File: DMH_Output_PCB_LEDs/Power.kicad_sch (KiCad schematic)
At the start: 79 parts, among them J0 Conn_01x01, J10 Conn_01x06, J100 IDC_02x05, J23 Conn_01x06, J29 Conn_01x01, U1 TL072, U10 NE5532, U11 TL074, U12 NE5532, U13 NE5532, U14 NE5532, U15 NE5532, U16 NE5532, U17 NE5532, U18 NE5532, U19 NE5532, U2 LM339, U20 TL072, U21 LM4040LP-10, U24 LM339, U25 LM339, U3 LM339, U4 LM339, U5 LM339, U6 LM339, U7 TL072, U8 TL074, U9 NE5532

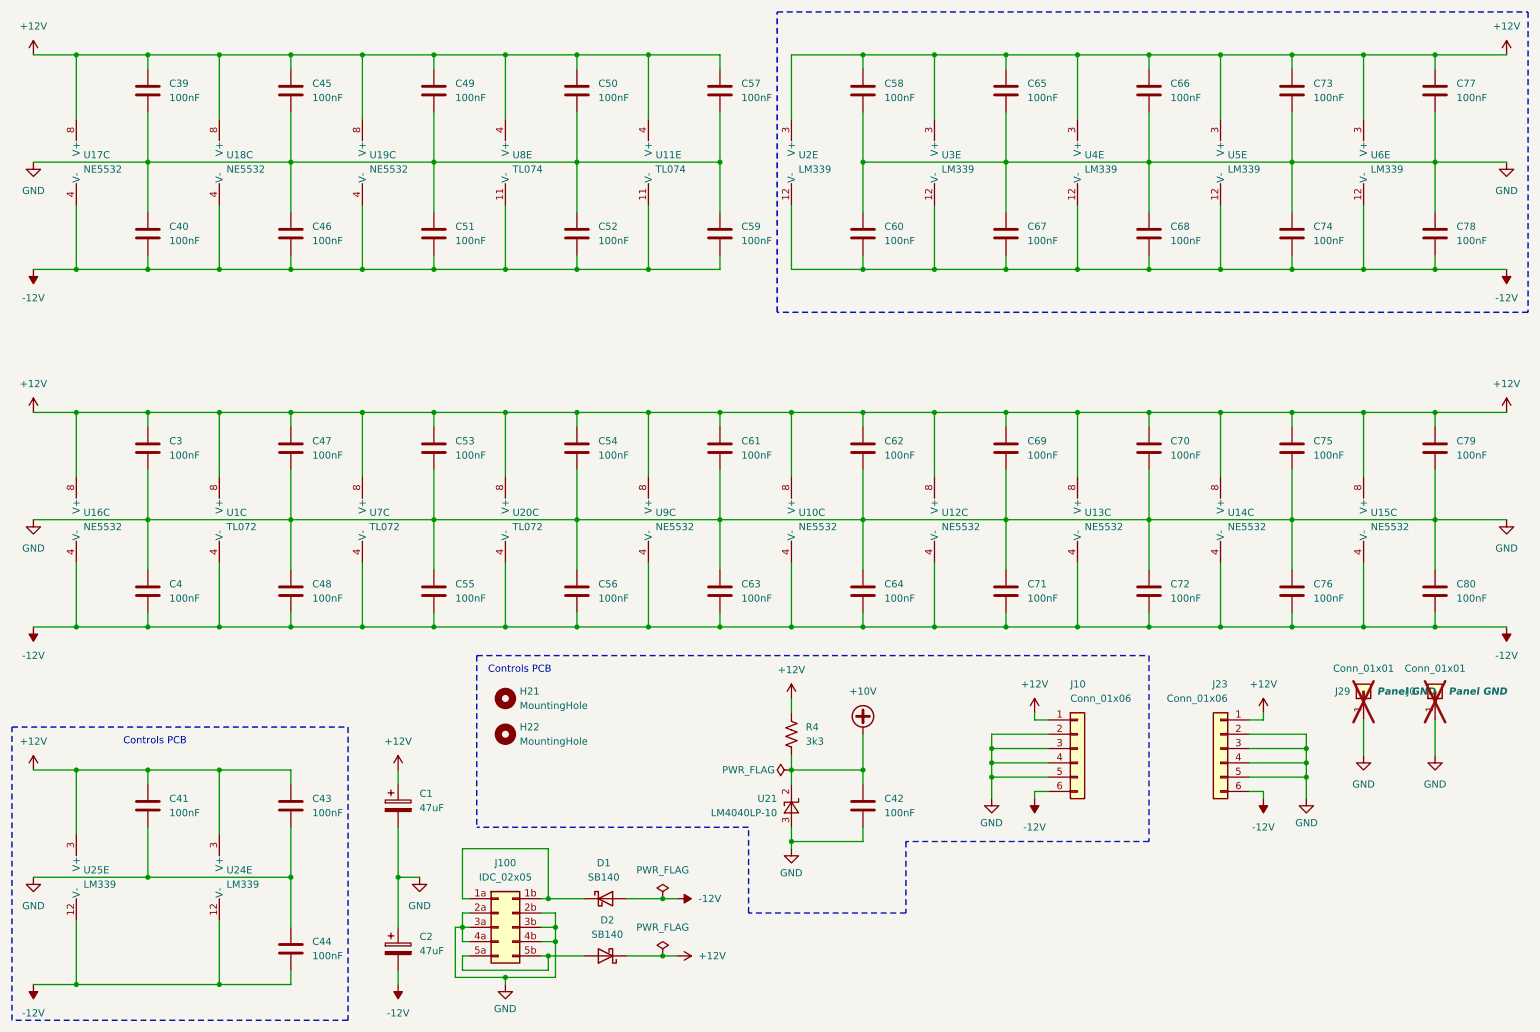
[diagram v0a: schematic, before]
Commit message: Adjusted output meter resistors
... and deleted unnecessary notes
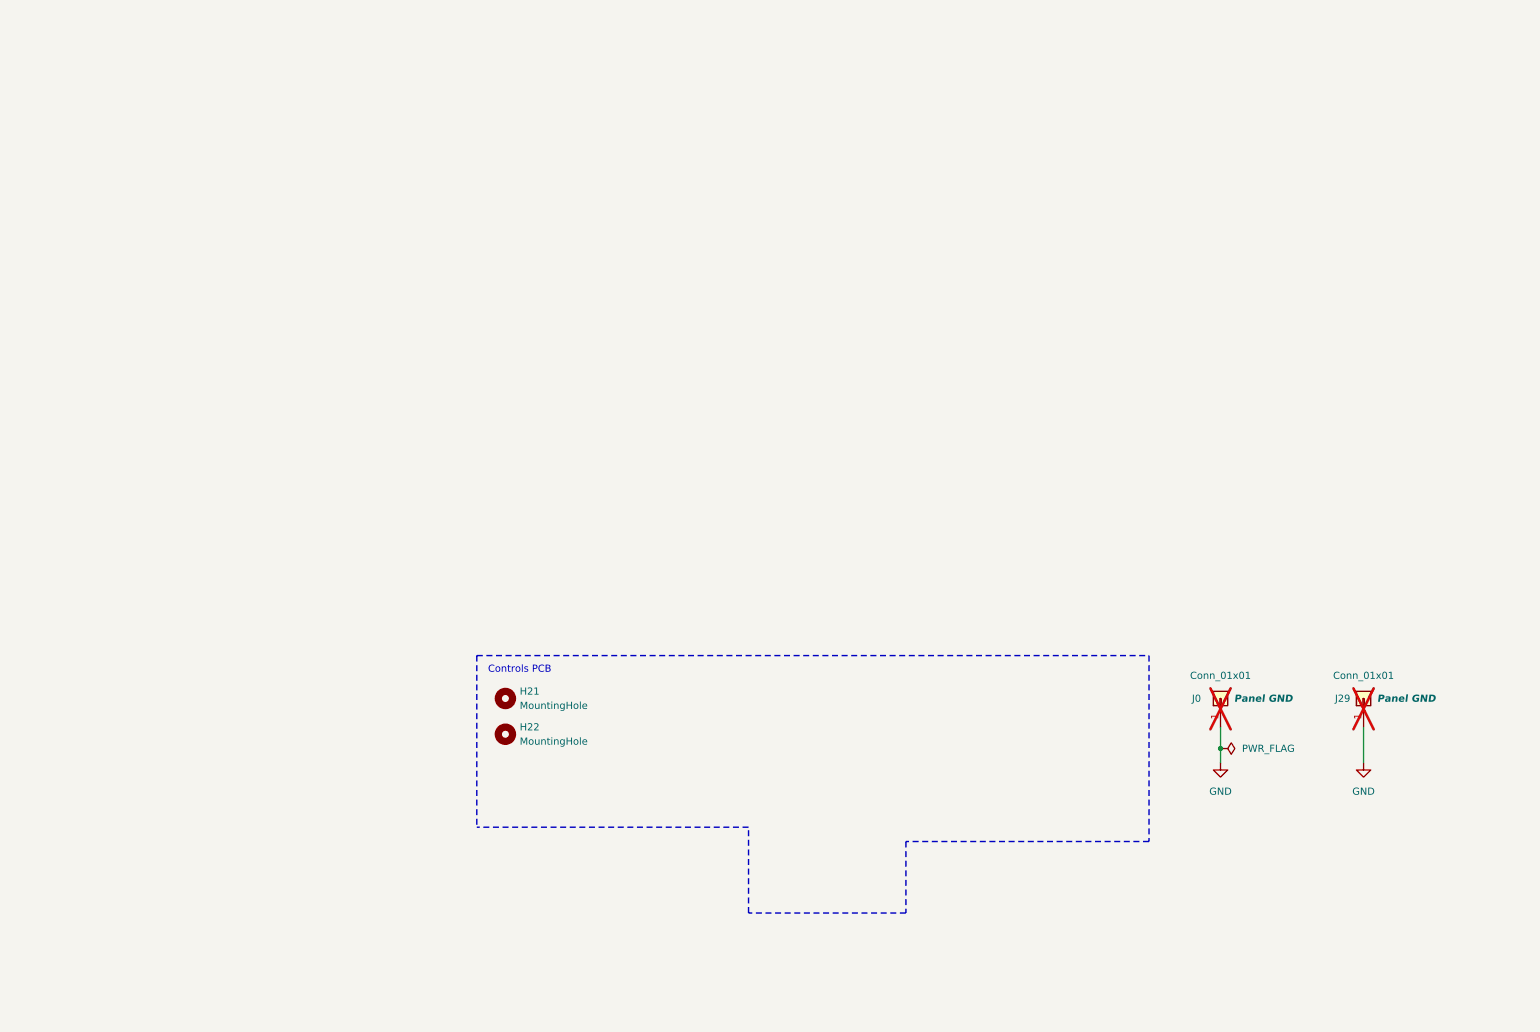
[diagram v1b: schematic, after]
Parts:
- removed C1, C2: 47uF, Capacitor_THT:CP_Radial_D5.0mm_P2.00mm, symbol Device:C_Polarized
- removed C3, C39, C4, C40, C41, C42, C43, C44, C45, C46, C47, C48, C49, C50, C51, C52, C53, C54, C55, C56, C57, C58, C59, C60, C61, C62, C63, C64, C65, C66, C67, C68, C69, C70, C71, C72, C73, C74, C75, C76, C77, C78, C79, C80: 100nF, Capacitor_THT:C_Disc_D4.3mm_W1.9mm_P5.00mm, symbol Device:C
- removed D1, D2: SB140, Diode_THT:D_DO-41_SOD81_P10.16mm_Horizontal, symbol Diode:SB140
- removed J10: Conn_01x06, Connector_PinSocket_2.54mm:PinSocket_1x06_P2.54mm_Vertical, symbol Connector_Generic:Conn_01x06
- removed J100: IDC_02x05, SynthStuff:IDC-Header_2x05_P2.54mm_Vertical_Eurorack, symbol SynthStuff:Eurorack_Power_Connector_10Pin
- removed J23: Conn_01x06, Connector_PinHeader_2.54mm:PinHeader_1x06_P2.54mm_Vertical, symbol Connector_Generic:Conn_01x06
- removed R4: 3k3, Resistor_THT:R_Axial_DIN0207_L6.3mm_D2.5mm_P7.62mm_Horizontal, symbol Device:R_US
- removed U1, U20, U7: TL072, Package_DIP:DIP-8_W7.62mm_Socket, symbol Amplifier_Operational:TL072
- removed U10, U12, U13, U14, U15, U16, U17, U18, U19, U9: NE5532, Package_DIP:DIP-8_W7.62mm_Socket, symbol Amplifier_Operational:NE5532
- removed U11, U8: TL074, Package_DIP:DIP-14_W7.62mm_Socket, symbol Amplifier_Operational:TL074
- removed U2, U24, U25, U3, U4, U5, U6: LM339, Package_DIP:DIP-14_W7.62mm_Socket, symbol Comparator:LM339
- removed U21: LM4040LP-10, Package_TO_SOT_THT:TO-92L_Inline_Wide, symbol Reference_Voltage:LM4040LP-10
